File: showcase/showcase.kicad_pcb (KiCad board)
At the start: 2 copper layers, 23 parts, among them J1 M_USB_B, SW1 SWITCH_INV

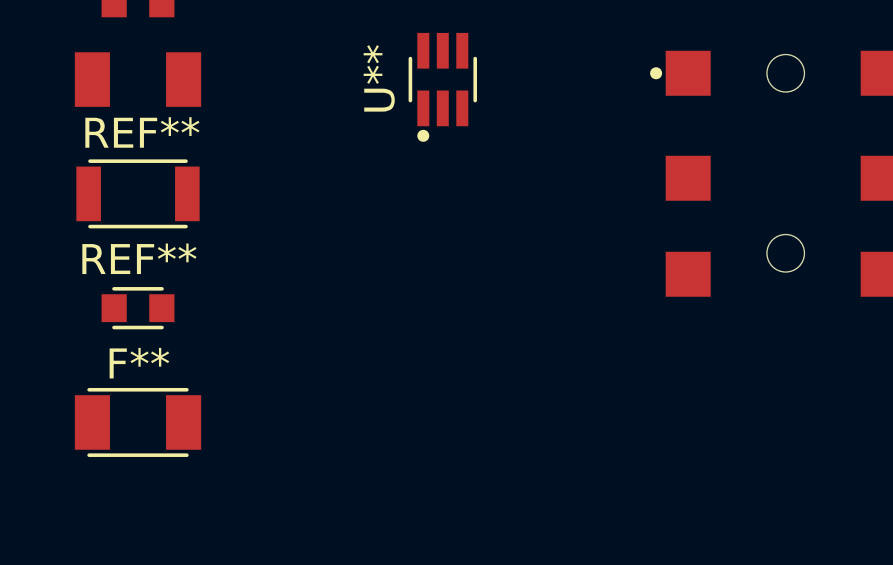
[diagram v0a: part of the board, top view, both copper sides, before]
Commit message: Added PAD footprint
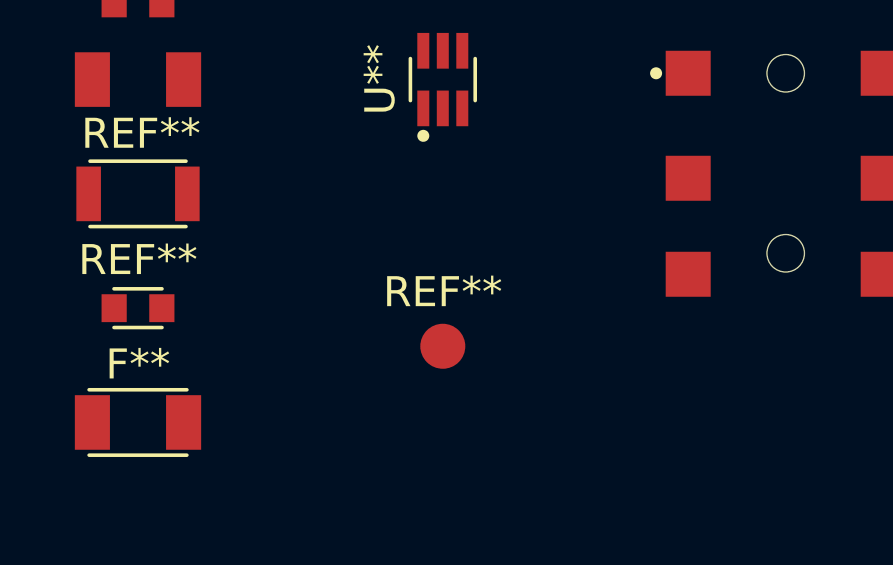
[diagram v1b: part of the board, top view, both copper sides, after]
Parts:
- added REF**: PAD_1_5MM, footprints:PAD_1_5MM, F.Cu at (27.9, 55.9)
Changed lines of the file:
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@@
     (tracks 0)
     (zones 0)
-    (modules 23)
+    (modules 24)
     (nets 1)
   )
@@
     (pad 7 thru_hole oval (at 3.575 0.85) (size 1.05 2.25) (drill oval 0.65 1.85) (layers *.Cu *.Mask F.Paste))
   )
+  (module footprints:PAD_1_5MM (layer F.Cu)
+    (at 27.94 55.88)
+    (fp_text reference REF** (at 0 -1.8) (layer F.SilkS)
+      (effects (font (size 1 1) (thickness 0.15)))
+    )
+    (fp_text value PAD_1_5MM (at 0 1.8) (layer F.Fab)
+      (effects (font (size 1 1) (thickness 0.15)))
+    )
+    (fp_circle (center 0 0) (end 1 0) (layer F.CrtYd) (width 0.05))
+    (pad 1 smd circle (at 0 0) (size 1.5 1.5) (layers F.Cu F.Paste F.Mask))
+  )
 )
